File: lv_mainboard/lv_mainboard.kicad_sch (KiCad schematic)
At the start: 63 parts, among them J1 Conn_01x02, J10 PWR, J11 Conn_02x05_Counter_Clockwise, J12 Conn_01x04, J13 Conn_02x10_Odd_Even, J14 Conn_01x04, J15 PWR, J16 Conn_01x04, J17 Conn_01x04, J18 Conn_01x02, J19 PWR, J2 Conn_02x10_Odd_Even, J3 Conn_01x03, J4 Conn_01x04, J5 Conn_01x05, J6 Conn_02x10_Odd_Even, J7 Conn_02x10_Odd_Even, J8 Conn_01x04, J9 DE9_Plug_MountingHoles, U1 AP2204K-ADJ, U2 AP2204K-ADJ, U3 AP2204K-ADJ

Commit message: v2025.8
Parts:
- removed C1, C3: 1u, Resistor_SMD:R_0603_1608Metric, symbol Device:C
- removed C2, C4: 10u, Resistor_SMD:R_0805_2012Metric, symbol Device:C
- removed C5: 1u, Capacitor_SMD:C_0603_1608Metric_Pad1.08x0.95mm_HandSolder, symbol Device:C_Small
- removed C6: 10u, Capacitor_SMD:C_0805_2012Metric_Pad1.18x1.45mm_HandSolder, symbol Device:C_Small
- removed J17: Conn_01x04, Connector_JST:JST_XH_B4B-XH-A_1x04_P2.50mm_Vertical, symbol Connector_Generic:Conn_01x04
- removed J9: DE9_Plug_MountingHoles, Connector_Dsub:DSUB-9_Female_Horizontal_P2.77x2.84mm_EdgePinOffset7.70mm_Housed_MountingHolesOffset9.12mm, symbol Connector:DE9_Plug_MountingHoles
- removed R3, R5: 100k, Resistor_SMD:R_0603_1608Metric, symbol Device:R
- removed R4: 301k, Resistor_SMD:R_0603_1608Metric, symbol Device:R
- removed R6: 165k, Resistor_SMD:R_0603_1608Metric, symbol Device:R
- removed R7: 100k, Resistor_SMD:R_0603_1608Metric, symbol Device:R_Small
- removed R8: 866k, Resistor_SMD:R_0603_1608Metric, symbol Device:R_Small
- removed TP1, TP2, TP3: TestPoint, TestPoint:TestPoint_THTPad_D1.5mm_Drill0.7mm, symbol Connector:TestPoint
- removed U1, U2, U3: AP2204K-ADJ, Package_TO_SOT_SMD:SOT-23-5, symbol Regulator_Linear:AP2204K-ADJ
- added J20, J21, J22: Conn_01x02, Connector_JST:JST_XH_B2B-XH-A_1x02_P2.50mm_Vertical, symbol Connector_Generic:Conn_01x02
- added J23: Conn_01x03, Connector_JST:JST_XH_B3B-XH-A_1x03_P2.50mm_Vertical, symbol Connector_Generic:Conn_01x03
- added J24, J9: PWR, Connector_AMASS:AMASS_XT60-M_1x02_P7.20mm_Vertical, symbol Connector_Generic:Conn_01x02
- added J25, J26, J27: Conn_01x04, Connector_JST:JST_XH_B4B-XH-A_1x04_P2.50mm_Vertical, symbol Connector_Generic:Conn_01x04
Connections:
- net SW_signal is gone; now on net SW_Fault: J2.2 (Pin_2)
- net +24V: now also J24.1 (Pin_1)
- net BMS_LED: now also J26.2 (Pin_2)
- net BMS_RST: now also J26.3 (Pin_3)
- net BSE_L_init: now also J21.2 (Pin_2)
- net BSE_R_init: now also J21.1 (Pin_1)
- net BSPD_LED: now also J25.2 (Pin_2)
- net BSPD_RST: now also J25.3 (Pin_3)
- net CAN+: now also J20.1 (Pin_1), J22.1 (Pin_1)
- net CAN-: now also J20.2 (Pin_2), J22.2 (Pin_2)
- net FAN_PWM: now also J23.2 (Pin_2)
- net FAN_PWR: now also J3.3 (Pin_3); no longer J3.2 (Pin_2)
- net GND: now also J7.11 (Pin_11), J7.13 (Pin_13), J7.15 (Pin_15), J7.17 (Pin_17), J7.5 (Pin_5), J7.7 (Pin_7), J7.9 (Pin_9), J23.1 (Pin_1), J24.2 (Pin_2), J25.1 (Pin_1), J26.1 (Pin_1), J27.1 (Pin_1), J9.2 (Pin_2)
- net IMD_LED: now also J27.2 (Pin_2)
- net IMD_RST: now also J27.3 (Pin_3)
- net P6_sideboard: now also J25.4 (Pin_4), J26.4 (Pin_4), J27.4 (Pin_4)
- net PUMP_PWM: now also J23.3 (Pin_3)
- net PUMP_PWR: now also J3.2 (Pin_2); no longer J3.3 (Pin_3)
- net P4_RGB renamed P4_HVbox
- net P4_HVbox: now also J9.1 (Pin_1)
- no-connect marks 4 -> 2
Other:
- note added: "24V to lv board(TSSI、RTML) fuse box 的走在上面"
- note added: "BSPD"
- note added: "Fuse + PWR"
- note added: "PWR 24V"
- note added: "SDC"
- note added: "rear MCU"
- note removed: "from HV box"
- moved on the sheet: H21, H22, H23, H24, J1, J10, J15, J18, J19, J3, J4, J5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

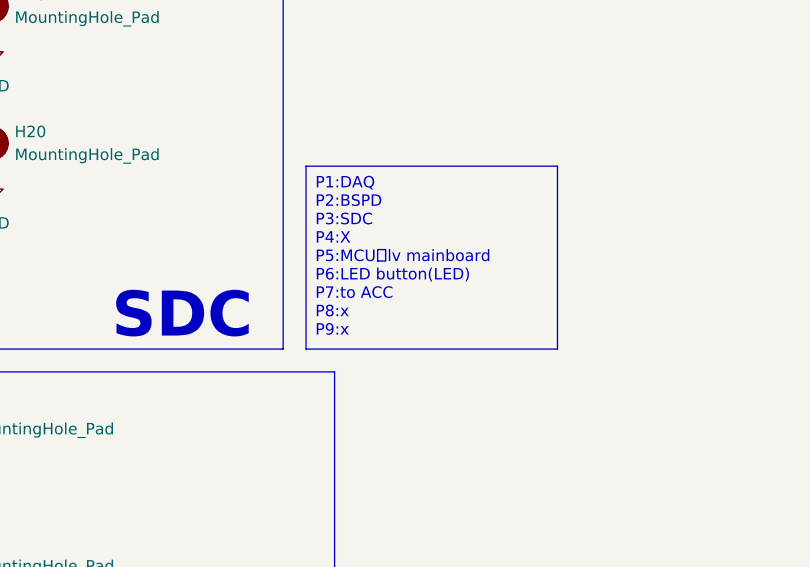
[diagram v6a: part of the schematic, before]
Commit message: v2025.8 but need to add another DAQ
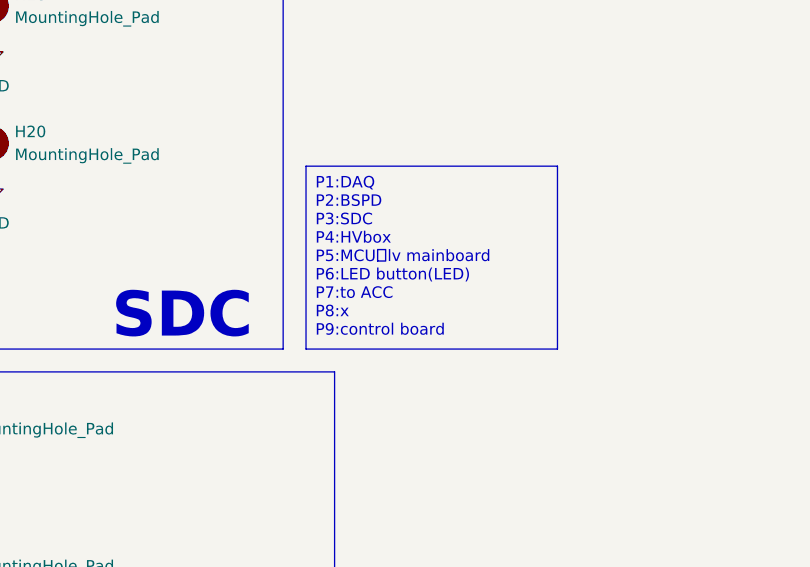
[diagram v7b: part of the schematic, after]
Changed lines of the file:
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@@
     (fill (type none))
   )
-  (text_box "P1:DAQ\nP2:BSPD\nP3:SDC\nP4:X\nP5:MCU、lv mainboard\nP6:LED button(LED)\nP7:to ACC\nP8:x\nP9:x"
+  (text_box "P1:DAQ\nP2:BSPD\nP3:SDC\nP4:HVbox\nP5:MCU、lv mainboard\nP6:LED button(LED)\nP7:to ACC\nP8:x\nP9:control board"
     (at 196.215 156.21 0) (size 27.94 20.32)
     (stroke (width 0) (type default))
